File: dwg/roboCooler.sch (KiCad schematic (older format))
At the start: 54 parts, among them J1 CONN_02X25, J10 CONN_01X12, J11 CONN_01X12, J12 CONN_01X04, J2 CONN_02X25, J3 CONN_01X04, J4 CONN_01X02, J5 CONN_01X02, J6 CONN_01X02, J7 CONN_01X02, J9 CONN_01X06, P1 CONN_01X03, P2 CONN_01X03, P3 USB_A, Q1 NMOS, Q2 NMOS, SW1 SPST_4PIN, SW2 SPST_4PIN, U1 SN74LV, U2 TB6549

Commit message: removed erc errors from schematic
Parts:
- removed J1, J2: CONN_02X25, roboCooler:Socket_Strip_Straight_2x25_Inverted, symbol CONN_02X25
- added J1: Discovery_F407_P1, roboCooler:Socket_Strip_Straight_2x25_Inverted, symbol Discovery_F407_P1
- added J2: Discovery_F407_P2, symbol Discovery_F407_P2
- P3: footprint (none) -> Connect:USB_A
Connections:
- wire segments 53 -> 55
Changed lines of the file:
@@
 $EndDescr
-$Comp
-L CONN_02X25 J1
-U 1 1 5664C6E0
-P 1475 3650
-F 0 "J1" H 1475 4950 50  0000 C CNN
-F 1 "CONN_02X25" V 1475 3650 50  0000 C CNN
-F 2 "roboCooler:Socket_Strip_Straight_2x25_Inverted" H 1475 2900 60  0001 C CNN
-F 3 "" H 1475 2900 60  0000 C CNN
-	1    1475 3650
-	1    0    0    -1
-$EndComp
-$Comp
-L CONN_02X25 J2
-U 1 1 5664C828
-P 3425 3650
-F 0 "J2" H 3425 4950 50  0000 C CNN
-F 1 "CONN_02X25" V 3425 3650 50  0000 C CNN
-F 2 "roboCooler:Socket_Strip_Straight_2x25_Inverted" H 3425 2900 60  0001 C CNN
-F 3 "" H 3425 2900 60  0000 C CNN
-	1    3425 3650
-	1    0    0    -1
-$EndComp
 $Comp
 L CONN_01X06 J9
@@
 	1    0    0    1
 $EndComp
-Wire Wire Line
-	5575 2300 5575 2400
-Wire Wire Line
-	5425 2150 5575 2150
-Wire Wire Line
-	5575 2350 5425 2350
-Connection ~ 5575 2350
-Wire Wire Line
-	6075 1375 6525 1375
-Wire Wire Line
-	5575 2150 5575 2200
-Wire Wire Line
-	2325 5600 2325 5675
-Wire Wire Line
-	3075 5600 3125 5600
-Wire Wire Line
-	3125 5600 3125 5675
-Wire Wire Line
-	3725 5600 3725 5675
-Wire Wire Line
-	1675 5600 1725 5600
-Wire Wire Line
-	1725 5600 1725 5675
-Wire Wire Line
-	975  6700 975  6900
-Wire Wire Line
-	975  6900 1925 6900
-Wire Wire Line
-	975  7000 1925 7000
-Wire Wire Line
-	1200 6700 1200 7000
-Connection ~ 1200 7000
-Wire Wire Line
-	5575 3425 5575 3525
-Wire Wire Line
-	5425 3275 5575 3275
-Wire Wire Line
-	5575 3475 5425 3475
-Connection ~ 5575 3475
-Wire Wire Line
-	5575 3275 5575 3325
-Wire Wire Line
-	10350 1750 10350 1900
-Wire Wire Line
-	9400 1525 9200 1525
-Wire Wire Line
-	9400 1600 8900 1600
-Wire Wire Line
-	8900 1600 8900 1525
-Wire Wire Line
-	9400 1450 9400 1200
-Wire Wire Line
-	9400 1200 9200 1200
-Wire Wire Line
-	10350 525  10350 1450
-Wire Wire Line
-	10575 825  11025 825
-Wire Wire Line
-	10775 1000 10775 825
-Connection ~ 10775 825
-Wire Wire Line
-	10650 1450 10825 1450
 $Comp
 L R R5
 U 1 1 57748645
 P 9400 2100
-F 0 "R5" V 9375 2275 50  0000 C CNN
+F 0 "R5" V 9450 1950 50  0000 C CNN
 F 1 "10k" V 9400 2100 50  0000 C CNN
 F 2 "Resistors_SMD:R_0805_HandSoldering" V 9330 2100 30  0001 C CNN
@@
 	-1   0    0    1
 $EndComp
-Wire Wire Line
-	8700 1675 9400 1675
 $Comp
 L R R4
 U 1 1 5774AB5E
 P 9300 2100
-F 0 "R4" V 9275 2275 50  0000 C CNN
+F 0 "R4" V 9350 1950 50  0000 C CNN
 F 1 "10k" V 9300 2100 50  0000 C CNN
 F 2 "Resistors_SMD:R_0805_HandSoldering" V 9230 2100 30  0001 C CNN
@@
 	-1   0    0    1
 $EndComp
-Wire Wire Line
-	8700 1825 9400 1825
-Wire Wire Line
-	9300 1825 9300 1950
 $Comp
 L R R3
 U 1 1 5774ADCD
 P 9200 2100
-F 0 "R3" V 9175 2275 50  0000 C CNN
+F 0 "R3" V 9250 1950 50  0000 C CNN
 F 1 "10k" V 9200 2100 50  0000 C CNN
 F 2 "Resistors_SMD:R_0805_HandSoldering" V 9130 2100 30  0001 C CNN
@@
 	-1   0    0    1
 $EndComp
-Wire Wire Line
-	8700 1750 9400 1750
-Wire Wire Line
-	9200 1750 9200 1950
 $Comp
 L R R2
 U 1 1 5774AF3C
 P 9100 2100
-F 0 "R2" V 9075 2275 50  0000 C CNN
+F 0 "R2" V 9150 1950 50  0000 C CNN
 F 1 "10k" V 9100 2100 50  0000 C CNN
 F 2 "Resistors_SMD:R_0805_HandSoldering" V 9030 2100 30  0001 C CNN
@@
 	-1   0    0    1
 $EndComp
-Wire Wire Line
-	9100 1675 9100 1950
-Wire Wire Line
-	9400 1900 9400 1950
 Text GLabel 8700 1600 0    60   Input ~ 0
 MOTOR_IN1
@@
 Text GLabel 8700 1975 0    60   Input ~ 0
 MOTOR_SB
-Wire Wire Line
-	10350 525  11025 525
-Connection ~ 10775 525
-Connection ~ 10575 525
-Wire Wire Line
-	8700 1675 8700 1600
-Connection ~ 9100 1675
-Wire Wire Line
-	8700 1750 8700 1725
-Connection ~ 9200 1750
-Wire Wire Line
-	8700 1825 8700 1850
-Connection ~ 9300 1825
-Wire Wire Line
-	9400 1900 8700 1900
-Wire Wire Line
-	8700 1900 8700 1975
 Text GLabel 3675 4150 2    60   Input ~ 0
 MOTOR_IN1
@@
 Text GLabel 10550 2250 2    60   Input ~ 0
 MOTOR_OUT2
-Wire Wire Line
-	10550 1600 10550 2250
-Wire Wire Line
-	10550 1600 10350 1600
-Wire Wire Line
-	10350 1675 10450 1675
-Wire Wire Line
-	10450 1675 10450 2375
-Wire Wire Line
-	10450 2375 10550 2375
 Text GLabel 9950 2725 0    60   Input ~ 0
 MOTOR_OUT1
 Text GLabel 9950 2925 0    60   Input ~ 0
 MOTOR_OUT2
-Wire Wire Line
-	10350 1525 10950 1525
-Wire Wire Line
-	10950 1525 10950 1600
-Connection ~ 10350 1825
 $Comp
 L +12V #PWR056
@@
 	0    1    -1   0
 $EndComp
-Wire Wire Line
-	5600 4500 5475 4500
 $Comp
 L R R7
@@
 	0    1    -1   0
 $EndComp
-Wire Wire Line
-	5525 5300 5600 5300
 $Comp
 L +5P #PWR057
@@
 F 0 "J6" H 750 850 50  0000 C CNN
 F 1 "CONN_01X02" V 850 700 50  0001 C CNN
-F 2 "" H 750 700 50  0000 C CNN
+F 2 "" H 750 700 50  0001 C CNN
 F 3 "" H 750 700 50  0000 C CNN
 	1    750  700
@@
 F 0 "J7" H 750 1300 50  0000 C CNN
 F 1 "CONN_01X02" V 850 1150 50  0001 C CNN
-F 2 "" H 750 1150 50  0000 C CNN
+F 2 "" H 750 1150 50  0001 C CNN
 F 3 "" H 750 1150 50  0000 C CNN
 	1    750  1150
@@
 F 0 "C16" H 1585 805 50  0000 L CNN
 F 1 "100uF" H 1560 670 50  0000 L CNN
-F 2 "" H 1550 750 50  0000 C CNN
+F 2 "" H 1550 750 50  0001 C CNN
 F 3 "" H 1550 750 50  0000 C CNN
 	1    1550 750
@@
 	1    0    0    -1
 $EndComp
-Wire Wire Line
-	1450 650  1925 650
 $Comp
 L C_Small C18
@@
 F 0 "C18" H 1735 805 50  0000 L CNN
 F 1 "100uF" H 1710 670 50  0000 L CNN
-F 2 "" H 1700 750 50  0000 C CNN
+F 2 "" H 1700 750 50  0001 C CNN
 F 3 "" H 1700 750 50  0000 C CNN
 	1    1700 750
@@
 	-1   0    0    -1
 $EndComp
-Connection ~ 1550 650
-Connection ~ 1700 650
 $Comp
 L C_Small C17
@@
 F 0 "C17" H 1585 1255 50  0000 L CNN
 F 1 "100uF" H 1560 1120 50  0000 L CNN
-F 2 "" H 1550 1200 50  0000 C CNN
+F 2 "" H 1550 1200 50  0001 C CNN
 F 3 "" H 1550 1200 50  0000 C CNN
 	1    1550 1200
@@
 	1    0    0    -1
 $EndComp
-Wire Wire Line
-	1450 1100 1925 1100
 $Comp
 L C_Small C19
@@
 F 0 "C19" H 1735 1255 50  0000 L CNN
 F 1 "100uF" H 1710 1120 50  0000 L CNN
-F 2 "" H 1700 1200 50  0000 C CNN
+F 2 "" H 1700 1200 50  0001 C CNN
 F 3 "" H 1700 1200 50  0000 C CNN
 	1    1700 1200
@@
 	-1   0    0    -1
 $EndComp
-Connection ~ 1550 1100
-Connection ~ 1700 1100
 $Comp
 L USB_A P3
@@
 F 0 "P3" V 550 1900 50  0000 C CNN
 F 1 "USB_A" H 800 2000 50  0000 C CNN
-F 2 "" V 800 1700 50  0000 C CNN
+F 2 "Connect:USB_A" V 800 1700 50  0001 C CNN
 F 3 "" V 800 1700 50  0000 C CNN
 	1    850  1800
@@
 Text Notes 1185 1790 0    60   ~ 0
 Alt Power for Disc Board
-NoConn ~ 1725 2650
 NoConn ~ 1725 2750
 NoConn ~ 1225 2850
@@
 NoConn ~ 3175 4250
 NoConn ~ 3175 4350
+$Comp
+L GND #PWR074
+U 1 1 578466F9
+P 9250 2250
+F 0 "#PWR074" H 9250 2000 50  0001 C CNN
+F 1 "GND" H 9250 2100 50  0000 C CNN
+F 2 "" H 9250 2250 60  0000 C CNN
+F 3 "" H 9250 2250 60  0000 C CNN
+	1    9250 2250
+	1    0    0    -1
+$EndComp
+Wire Wire Line
+	5575 2300 5575 2400
+Wire Wire Line
+	5425 2150 5575 2150
+Wire Wire Line
+	5575 2350 5425 2350
+Connection ~ 5575 2350
+Wire Wire Line
+	6075 1375 6525 1375
+Wire Wire Line
+	5575 2150 5575 2200
+Wire Wire Line
+	2325 5600 2325 5675
+Wire Wire Line
+	3075 5600 3125 5600
+Wire Wire Line
+	3125 5600 3125 5675
+Wire Wire Line
+	3725 5600 3725 5675
+Wire Wire Line
+	1675 5600 1725 5600
+Wire Wire Line
+	1725 5600 1725 5675
+Wire Wire Line
+	975  6700 975  6900
+Wire Wire Line
+	975  6900 1925 6900
+Wire Wire Line
+	975  7000 1925 7000
+Wire Wire Line
+	1200 6700 1200 7000
+Connection ~ 1200 7000
+Wire Wire Line
+	5575 3425 5575 3525
+Wire Wire Line
+	5425 3275 5575 3275
+Wire Wire Line
+	5575 3475 5425 3475
+Connection ~ 5575 3475
+Wire Wire Line
+	5575 3275 5575 3325
+Wire Wire Line
+	10350 1750 10350 1900
+Wire Wire Line
+	9400 1525 9200 1525
+Wire Wire Line
+	9400 1600 8900 1600
+Wire Wire Line
+	8900 1600 8900 1525
+Wire Wire Line
+	9400 1450 9400 1200
+Wire Wire Line
+	9400 1200 9200 1200
+Wire Wire Line
+	10350 525  10350 1450
+Wire Wire Line
+	10575 825  11025 825
+Wire Wire Line
+	10775 1000 10775 825
+Connection ~ 10775 825
+Wire Wire Line
+	10650 1450 10825 1450
+Wire Wire Line
+	8700 1675 9400 1675
+Wire Wire Line
+	8700 1825 9400 1825
+Wire Wire Line
+	9300 1825 9300 1950
+Wire Wire Line
+	8700 1750 9400 1750
+Wire Wire Line
+	9200 1750 9200 1950
+Wire Wire Line
+	9100 1675 9100 1950
+Wire Wire Line
+	9400 1900 9400 1950
+Wire Wire Line
+	10350 525  11025 525
+Connection ~ 10775 525
+Connection ~ 10575 525
+Wire Wire Line
+	8700 1675 8700 1600
+Connection ~ 9100 1675
+Wire Wire Line
+	8700 1750 8700 1725
+Connection ~ 9200 1750
+Wire Wire Line
+	8700 1825 8700 1850
+Connection ~ 9300 1825
+Wire Wire Line
+	9400 1900 8700 1900
+Wire Wire Line
+	8700 1900 8700 1975
+Wire Wire Line
+	10550 1600 10550 2250
+Wire Wire Line
+	10550 1600 10350 1600
+Wire Wire Line
+	10350 1675 10450 1675
+Wire Wire Line
+	10450 1675 10450 2375
+Wire Wire Line
+	10450 2375 10550 2375
+Wire Wire Line
+	10350 1525 10950 1525
+Wire Wire Line
+	10950 1525 10950 1600
+Connection ~ 10350 1825
+Wire Wire Line
+	5600 4500 5475 4500
+Wire Wire Line
+	5525 5300 5600 5300
+Wire Wire Line
+	1450 650  1925 650
+Connection ~ 1550 650
+Connection ~ 1700 650
+Wire Wire Line
+	1450 1100 1925 1100
+Connection ~ 1550 1100
+Connection ~ 1700 1100
+Wire Wire Line
+	9100 2250 9400 2250
+Wire Wire Line
+	9200 2250 9300 2250
+Connection ~ 9300 2250
+Connection ~ 9200 2250
+Connection ~ 9250 2250
+$Comp
+L Discovery_F407_P1 J1
+U 1 1 5784F5D3
+P 1475 3650
+F 0 "J1" H 1475 4950 50  0000 C CNN
+F 1 "Discovery_F407_P1" V 1475 3650 50  0000 C CNN
+F 2 "roboCooler:Socket_Strip_Straight_2x25_Inverted" H 1475 2900 50  0001 C CNN
+F 3 "" H 1475 2900 50  0000 C CNN
+	1    1475 3650
+	1    0    0    -1
+$EndComp
+NoConn ~ 1725 2650
+$Comp
+L Discovery_F407_P2 J2
+U 1 1 57856C7E
+P 3425 3650
+F 0 "J2" H 3425 4950 50  0000 C CNN
+F 1 "Discovery_F407_P2" V 3425 3650 50  0000 C CNN
+F 2 "" H 3425 2900 50  0000 C CNN
+F 3 "" H 3425 2900 50  0000 C CNN
+	1    3425 3650
+	1    0    0    -1
+$EndComp
 $EndSCHEMATC

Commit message: reset layout
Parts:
- J6: renamed from J2; footprint (none) -> roboCooler:Socket_Strip_Straight_2x25_Inverted
- renumbered C16 to C1, C4 to C10, C6 to C11, C8 to C12, C9 to C13, C10 to C14, C11 to C15, C12 to C16, C13 to C17, C14 to C18, C15 to C19, C17 to C2, C18 to C3, C19 to C4, C1 to C5, C3 to C6, C5 to C7, C7 to C8, C2 to C9, F2 to F1, F3 to F2, J6 to J1, J3 to J10, J12 to J11, J7 to J2, J1 to J3, J9 to J4, J10 to J5, J11 to J7, J5 to J8, J4 to J9, P3 to P1, P1 to P2, P2 to P3, R14 to R1, R4 to R10, R5 to R11, R15 to R2, R12 to R3, R13 to R4, R6 to R5, R7 to R6, R1 to R7, R2 to R8, R3 to R9

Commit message: Initial part placement on layout complete
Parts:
- removed C19: CP1, symbol CP1
- added C19: 1UF, Capacitors_SMD:C_0805_HandSoldering, symbol C
- C1, C2, C3, C4: footprint (none) -> roboCooler:c_elec_6.6x6.6
- C16: value ??UF -> 10UF
- C17: value ??UF -> .01UF
- C5: footprint TO_SOT_Packages_SMD:TO-263-3Lead -> Capacitors_SMD:C_0805_HandSoldering
- J1, J2: footprint (none) -> Pin_Headers:Pin_Header_Angled_1x02
- J11: footprint (none) -> Socket_Strips:Socket_Strip_Angled_1x04
- renumbered P1 to J12
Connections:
- wire segments 55 -> 56
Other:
- moved on the sheet: C15, C16

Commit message: updated BOM
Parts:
- renumbered P2 to J13, P3 to J14

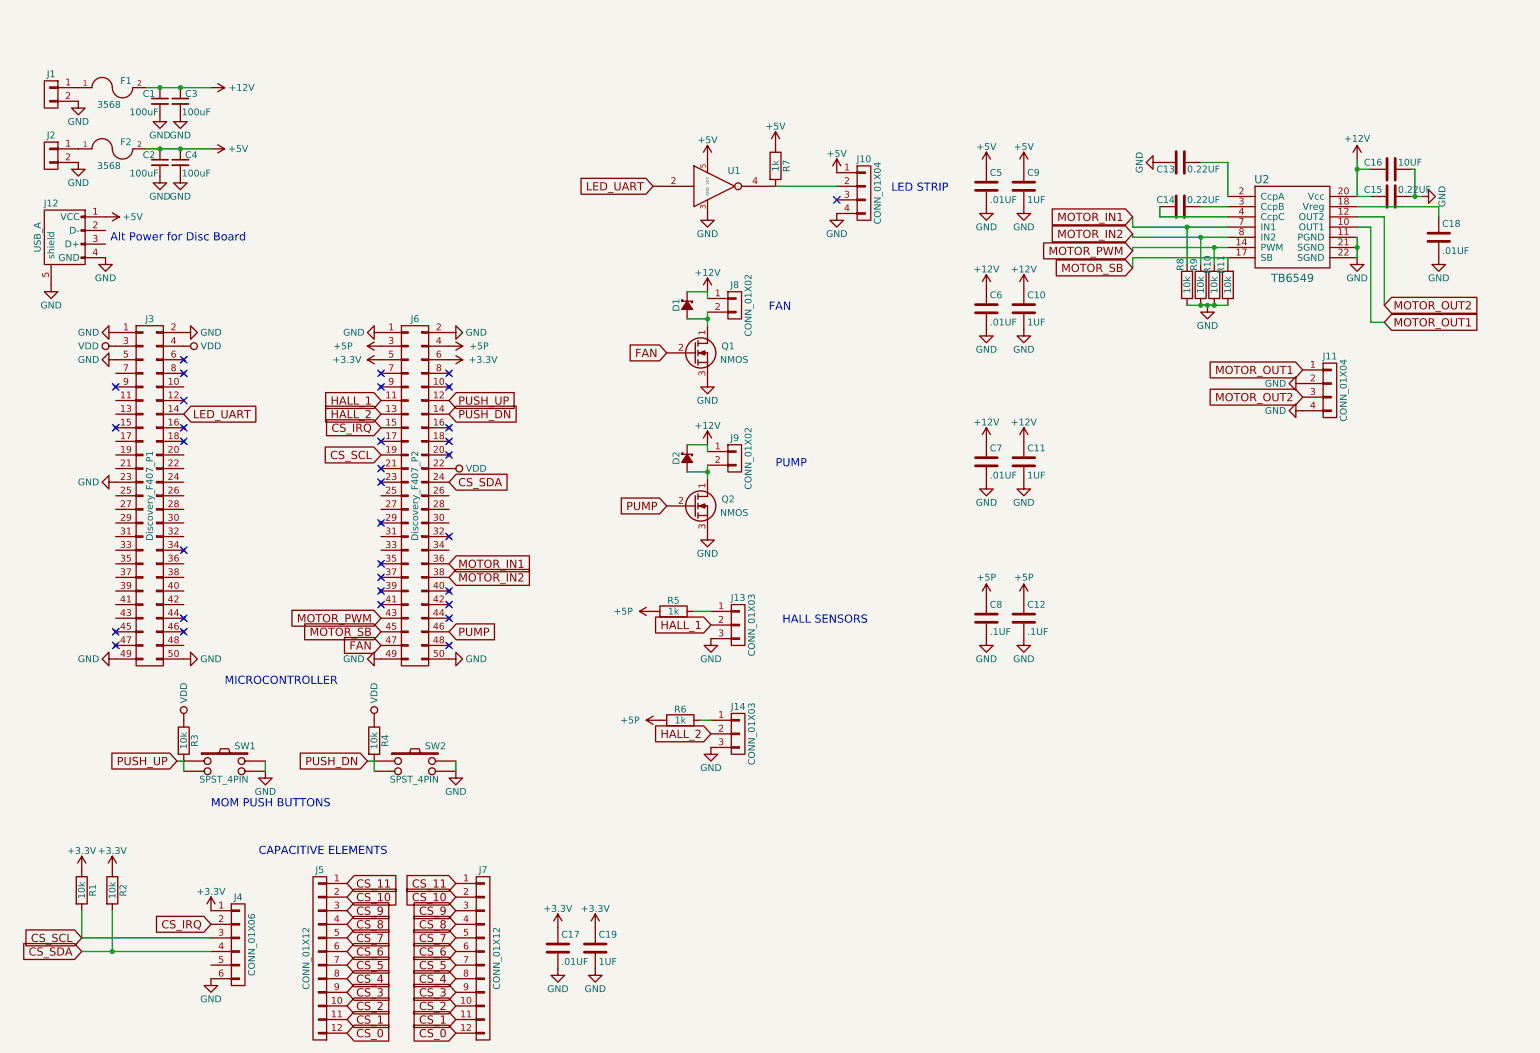
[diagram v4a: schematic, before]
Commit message: updated conn for capsense out and hal sensors
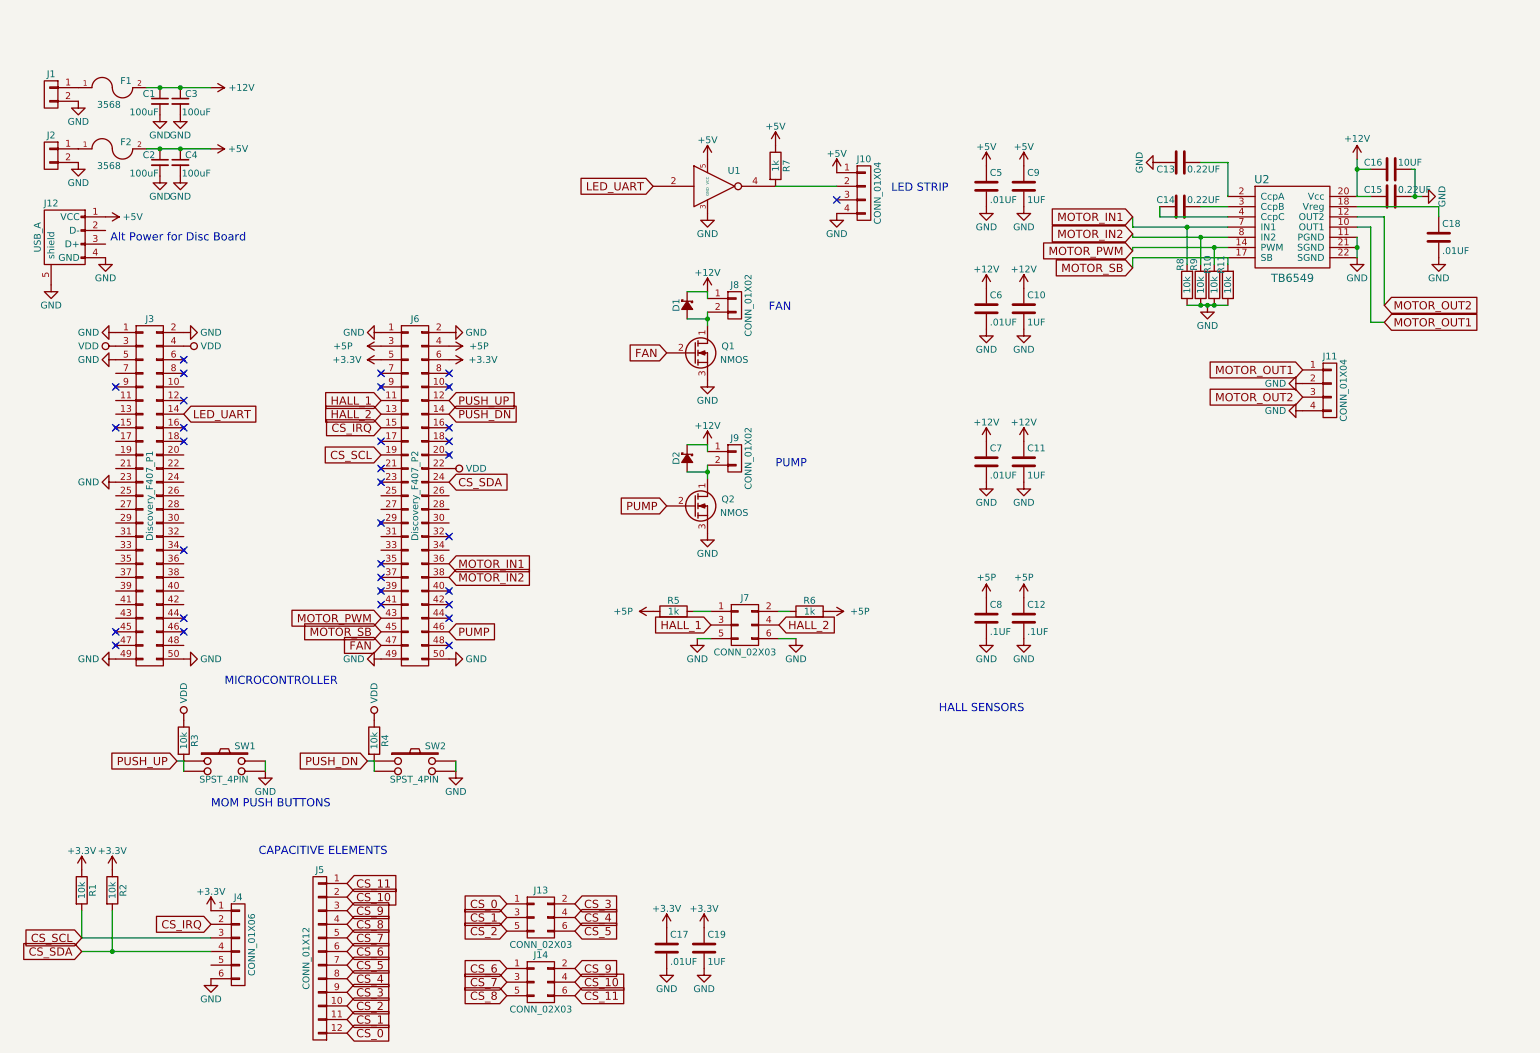
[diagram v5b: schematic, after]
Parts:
- removed J13, J14: CONN_01X03, Socket_Strips:Socket_Strip_Angled_1x03, symbol CONN_01X03
- removed J7: CONN_01X12, Socket_Strips:Socket_Strip_Angled_1x12, symbol CONN_01X12
- added J13, J14, J7: CONN_02X03, Pin_Headers:Pin_Header_Angled_2x03, symbol CONN_02X03
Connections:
- net CS_0: now also J13.1 (P1)
- net CS_1: now also J13.3 (P3)
- net CS_10: now also J14.4 (P4)
- net CS_11: now also J14.6 (P6)
- net CS_2: now also J13.5 (P5)
- net CS_3: now also J13.2 (P2)
- net CS_4: now also J13.4 (P4)
- net CS_5: now also J13.6 (P6)
- net CS_6: now also J14.1 (P1)
- net CS_7: now also J14.3 (P3)
- net CS_8: now also J14.5 (P5)
- net CS_9: now also J14.2 (P2)
- net GND: now also J7.5 (P5), J7.6 (P6)
- net HALL_1: now also J7.3 (P3)
- net HALL_2: now also J7.4 (P4)
- net at R5.1: now also J7.1 (P1)
- net at R6.1: now also J7.2 (P2)
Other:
- moved on the sheet: C17, C19, R6
